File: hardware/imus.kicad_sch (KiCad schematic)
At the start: 11 parts, among them U4 ASM330LHHX, U6 IIS2MDCTR

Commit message: Please Final Review
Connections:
- no-connect marks 2 -> 4
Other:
- note added: "3-Axis Magnetometer"
- note added: "6-Axis IMU"
- moved on the sheet: C25, C26, C27, C28, C40, C41, R24, R25, R26, U4, U6

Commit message: PLEASE FINAL REVIEW
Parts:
- U6: now not fitted
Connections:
- net 3.3V: now also C40.2; no longer C40.1
- net GND: now also C40.1; no longer C40.2
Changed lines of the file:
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@@
 	)
 	(junction
+		(at 256.54 31.75)
+		(diameter 0)
+		(color 0 0 0 0)
+	)
+	(junction
 		(at 160.02 43.18)
 		(diameter 0)
@@
 		(color 0 0 0 0)
 	)
-	(junction
-		(at 257.81 40.64)
-		(diameter 0)
-		(color 0 0 0 0)
-	)
 	(no_connect
 		(at 90.17 46.99)
@@
 	(wire
 		(pts
+			(xy 256.54 39.37) (xy 260.35 39.37)
+		)
+		(stroke
+			(width 0)
+			(type default)
+		)
+	)
+	(wire
+		(pts
 			(xy 257.81 43.18) (xy 266.7 43.18)
 		)
@@
 	(wire
 		(pts
+			(xy 252.73 31.75) (xy 256.54 31.75)
+		)
+		(stroke
+			(width 0)
+			(type default)
+		)
+	)
+	(wire
+		(pts
 			(xy 158.75 43.18) (xy 160.02 43.18)
 		)
@@
 	(wire
 		(pts
+			(xy 252.73 40.64) (xy 252.73 31.75)
+		)
+		(stroke
+			(width 0)
+			(type default)
+		)
+	)
+	(wire
+		(pts
 			(xy 44.45 39.37) (xy 39.37 39.37)
 		)
@@
 	(wire
 		(pts
-			(xy 254 33.02) (xy 257.81 33.02)
-		)
-		(stroke
-			(width 0)
-			(type default)
-		)
-	)
-	(wire
-		(pts
-			(xy 257.81 40.64) (xy 266.7 40.64)
+			(xy 238.76 40.64) (xy 252.73 40.64)
 		)
 		(stroke
@@
 	(wire
 		(pts
-			(xy 238.76 40.64) (xy 257.81 40.64)
+			(xy 256.54 31.75) (xy 266.7 31.75)
 		)
 		(stroke
@@
 	)
 	(image
-		(at 63.5 149.86)
-		(scale 0.313825)
+		(at 74.93 147.32)
+		(scale 0.384416)
 		(data "iVBORw0KGgoAAAANSUhEUgAABnIAAAT4CAYAAAAsDFyTAAAMUmlDQ1BJQ0MgUHJvZmlsZQAASImV"
 			"VwdYU8kWnlvSgNACCEgJvYkiUgJICT303kQlJAFCCTEhqIgNXVRwLahYsKKLIgpWmh0bKoti74sF"
@@
 		)
 	)
-	(hierarchical_label "3.3V"
-		(shape input)
-		(at 266.7 40.64 0)
-		(effects
-			(font
-				(size 1.27 1.27)
-			)
-			(justify left)
-		)
-	)
 	(hierarchical_label "GND"
 		(shape bidirectional)
@@
 	(hierarchical_label "GND"
 		(shape bidirectional)
-		(at 254 33.02 180)
+		(at 260.35 39.37 0)
 		(effects
 			(font
 				(size 1.27 1.27)
 			)
-			(justify right)
+			(justify left)
 		)
 	)
@@
 		)
 	)
+	(hierarchical_label "3.3V"
+		(shape input)
+		(at 266.7 31.75 0)
+		(effects
+			(font
+				(size 1.27 1.27)
+			)
+			(justify left)
+		)
+	)
 	(hierarchical_label "SPI_MOSI"
 		(shape output)
@@
 	(symbol
 		(lib_id "Device:C")
+		(at 256.54 35.56 180)
+		(unit 1)
+		(body_style 1)
+		(exclude_from_sim no)
+		(in_bom yes)
+		(on_board yes)
+		(in_pos_files yes)
+		(dnp no)
+		(property "Reference" "C40"
+			(at 261.62 34.036 0)
+			(show_name no)
+			(do_not_autoplace no)
+			(effects
+				(font
+					(size 1.27 1.27)
+				)
+				(justify right)
+			)
+		)
+		(property "Value" "100nF"
+			(at 259.08 36.322 0)
+			(show_name no)
+			(do_not_autoplace no)
+			(effects
+				(font
+					(size 1.27 1.27)
+				)
+				(justify right)
+			)
+		)
+		(property "Footprint" "RF_Converter:Balun_Johanson_0900PC15J0013"
+			(at 255.5748 31.75 0)
+			(hide yes)
+			(show_name no)
+			(do_not_autoplace no)
+			(effects
+				(font
+					(size 1.27 1.27)
+				)
+			)
+		)
+		(property "Datasheet" ""
+			(at 256.54 35.56 0)
+			(hide yes)
+			(show_name no)
+			(do_not_autoplace no)
+			(effects
+				(font
+					(size 1.27 1.27)
+				)
+			)
+		)
+		(property "Description" "Unpolarized capacitor"
+			(at 256.54 35.56 0)
+			(hide yes)
+			(show_name no)
+			(do_not_autoplace no)
+			(effects
+				(font
+					(size 1.27 1.27)
+				)
+			)
+		)
+		(pin "2"
+		)
+		(pin "1"
+		)
+		(instances
+			(project "wheelsBoard"
+				(path "/69127114-6359-479f-a1a1-af440f90be3d/b6e3f34b-784c-4fc1-b618-c3e17c431e68"
+					(reference "C40")
+					(unit 1)
+				)
+			)
+		)
+	)
+	(symbol
+		(lib_id "Device:C")
 		(at 257.81 46.99 180)
 		(unit 1)
@@
 		(on_board yes)
 		(in_pos_files yes)
-		(dnp no)
+		(dnp yes)
 		(fields_autoplaced yes)
 		(property "Reference" "U6"
@@
 					(unit 1)
 				)
-			)
-		)
-	)
-	(symbol
-		(lib_id "Device:C")
-		(at 257.81 36.83 180)
-		(unit 1)
-		(body_style 1)
-		(exclude_from_sim no)
-		(in_bom yes)
-		(on_board yes)
-		(in_pos_files yes)
-		(dnp no)
-		(property "Reference" "C40"
-			(at 262.89 35.306 0)
-			(show_name no)
-			(do_not_autoplace no)
-			(effects
-				(font
-					(size 1.27 1.27)
-				)
-				(justify right)
-			)
-		)
-		(property "Value" "100nF"
-			(at 260.35 37.592 0)
-			(show_name no)
-			(do_not_autoplace no)
-			(effects
-				(font
-					(size 1.27 1.27)
-				)
-				(justify right)
-			)
-		)
-		(property "Footprint" "RF_Converter:Balun_Johanson_0900PC15J0013"
-			(at 256.8448 33.02 0)
-			(hide yes)
-			(show_name no)
-			(do_not_autoplace no)
-			(effects
-				(font
-					(size 1.27 1.27)
-				)
-			)
-		)
-		(property "Datasheet" ""
-			(at 257.81 36.83 0)
-			(hide yes)
-			(show_name no)
-			(do_not_autoplace no)
-			(effects
-				(font
-					(size 1.27 1.27)
-				)
-			)
-		)
-		(property "Description" "Unpolarized capacitor"
-			(at 257.81 36.83 0)
-			(hide yes)
-			(show_name no)
-			(do_not_autoplace no)
-			(effects
-				(font
-					(size 1.27 1.27)
-				)
-			)
-		)
-		(pin "2"
-		)
-		(pin "1"
-		)
-		(instances
-			(project "wheelsBoard"
-				(path "/69127114-6359-479f-a1a1-af440f90be3d/b6e3f34b-784c-4fc1-b618-c3e17c431e68"
-					(reference "C40")
-					(unit 1)
-				)

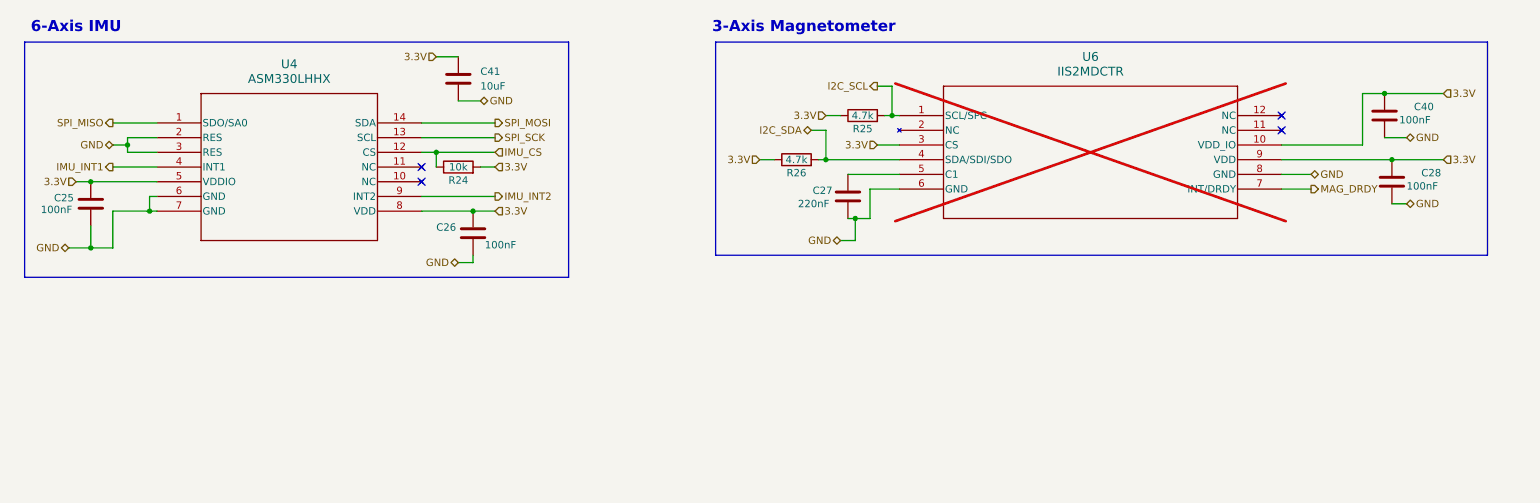
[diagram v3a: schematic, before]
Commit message: Changed MAG to SPI
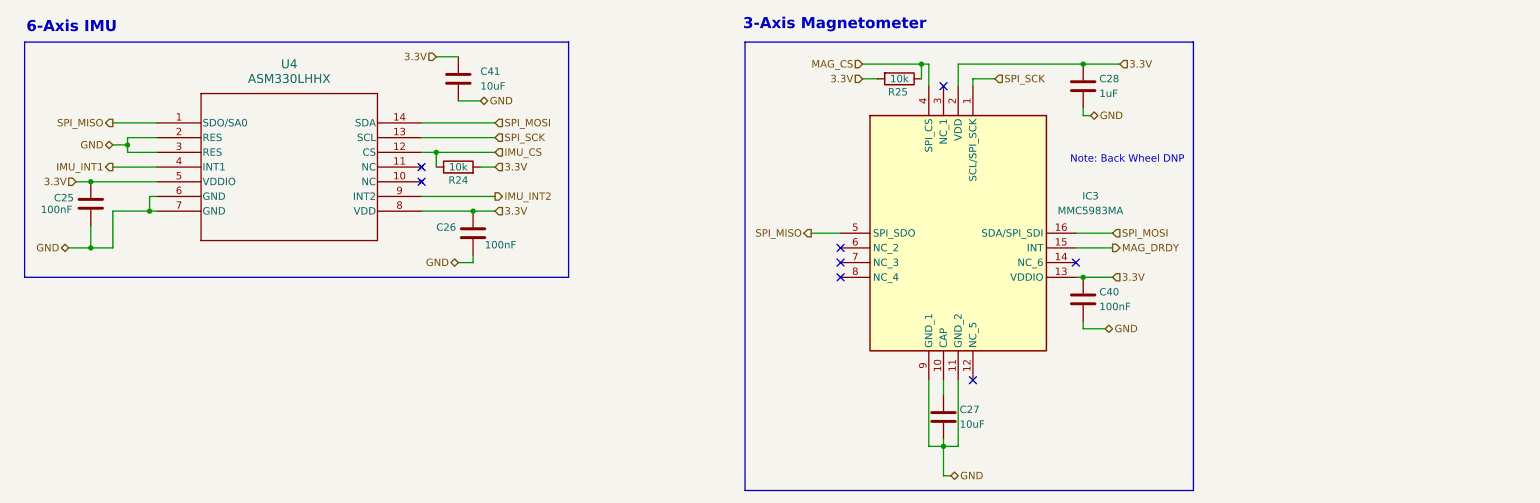
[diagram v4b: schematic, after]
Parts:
- removed R26: 4.7k, symbol Device:R
- removed U6: IIS2MDCTR, LGA-12_2X2X0P7_STM, symbol 2026-10-07_23-27-46:IIS2MDCTR
- added IC3: MMC5983MA, MMC5983MA:MMC5983MA, symbol MMC5983MA:MMC5983MA
- C27: value 220nF -> 10uF; footprint RF_Converter:Balun_Johanson_0900PC15J0013 -> (none)
- C28: value 100nF -> 1uF; footprint RF_Converter:Balun_Johanson_0900PC15J0013 -> (none)
- C40: footprint RF_Converter:Balun_Johanson_0900PC15J0013 -> (none)
- R25: value 4.7k -> 10k
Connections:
- net I2C_SCL is gone; now on net 3.3V: R25.2
- net 3.3V: now also C28.1, C40.1, IC3.13 (VDDIO), IC3.2 (VDD); no longer C28.2, C40.2, R25.1
- net GND: now also C27.2, C28.2, C40.2, IC3.11 (GND_2), IC3.9 (GND_1); no longer C27.1, C28.1, C40.1
- net MAG_DRDY: now also IC3.15 (INT)
- net SPI_MISO: now also IC3.5 (SPI_SDO)
- net SPI_MOSI: now also IC3.16 (SDA/SPI_SDI)
- net SPI_SCK: now also IC3.1 (SCL/SPI_SCK)
- new net: C27.1, IC3.10 (CAP)
- new net MAG_CS: IC3.4 (SPI_CS), R25.1
- no-connect marks 4 -> 8
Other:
- note added: "Note: Back Wheel DNP"
